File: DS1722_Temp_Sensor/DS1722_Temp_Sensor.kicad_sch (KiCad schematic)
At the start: 13 parts, among them J1 Conn_01x08, J2 Conn_01x08

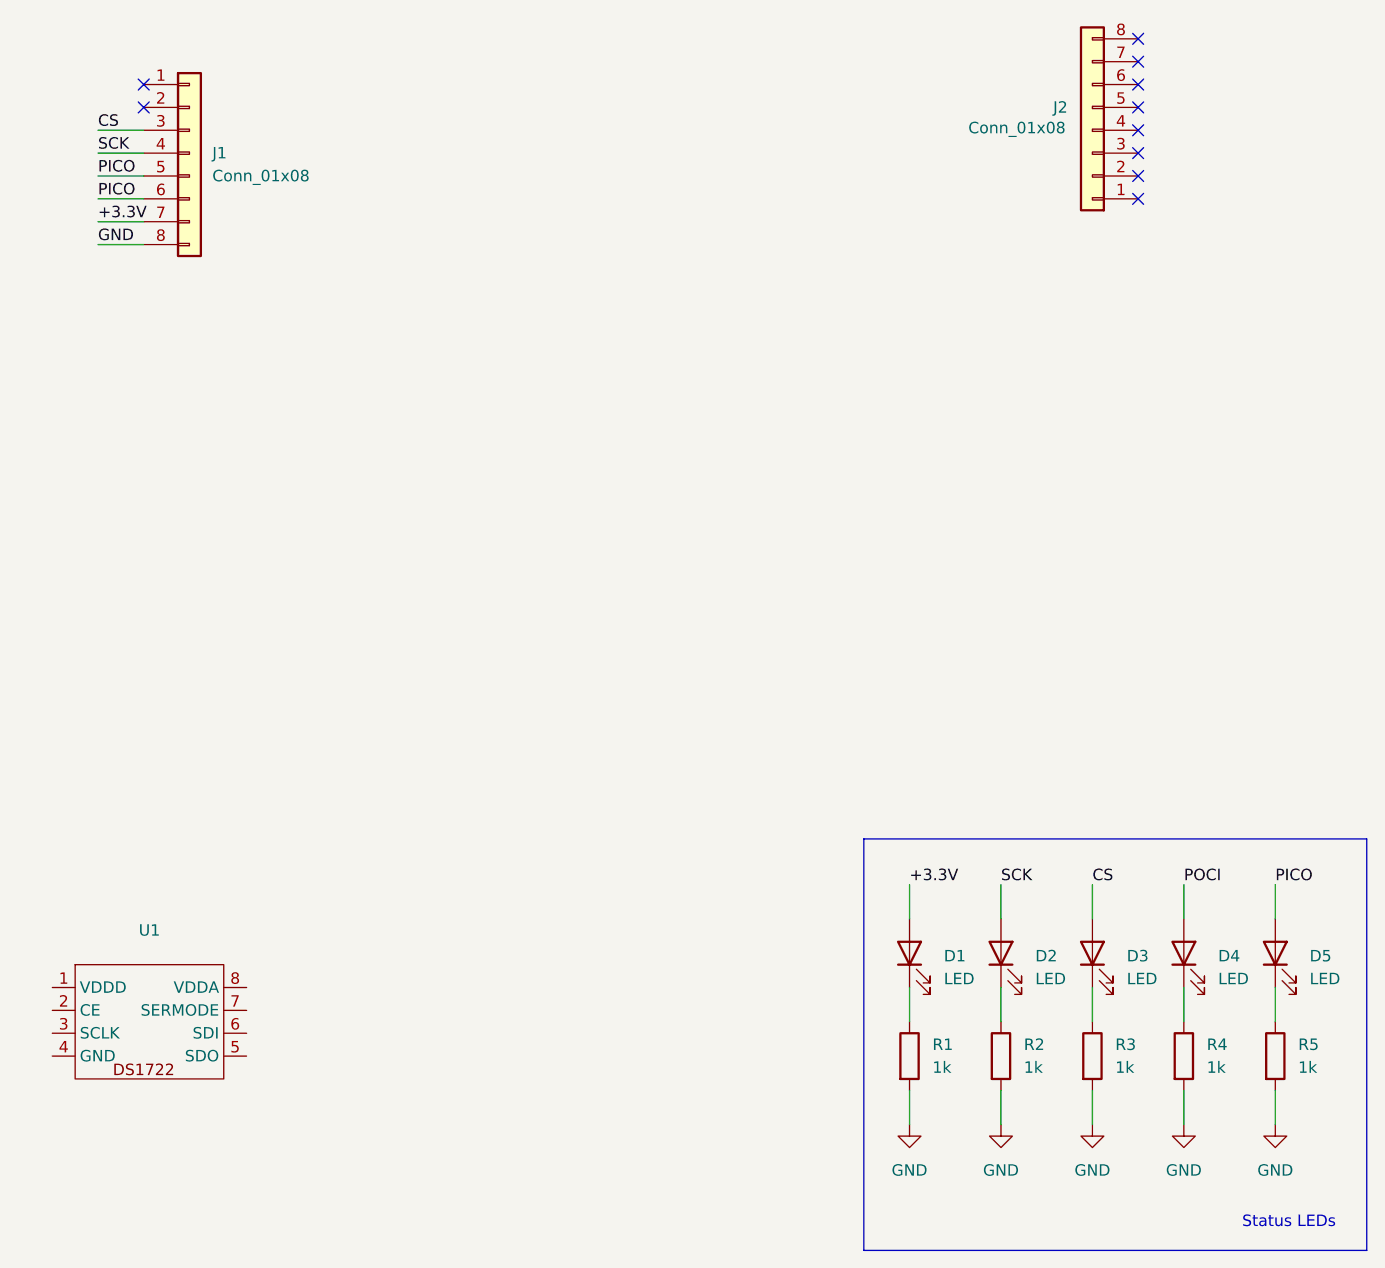
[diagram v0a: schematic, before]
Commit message: Added in labels in schematic
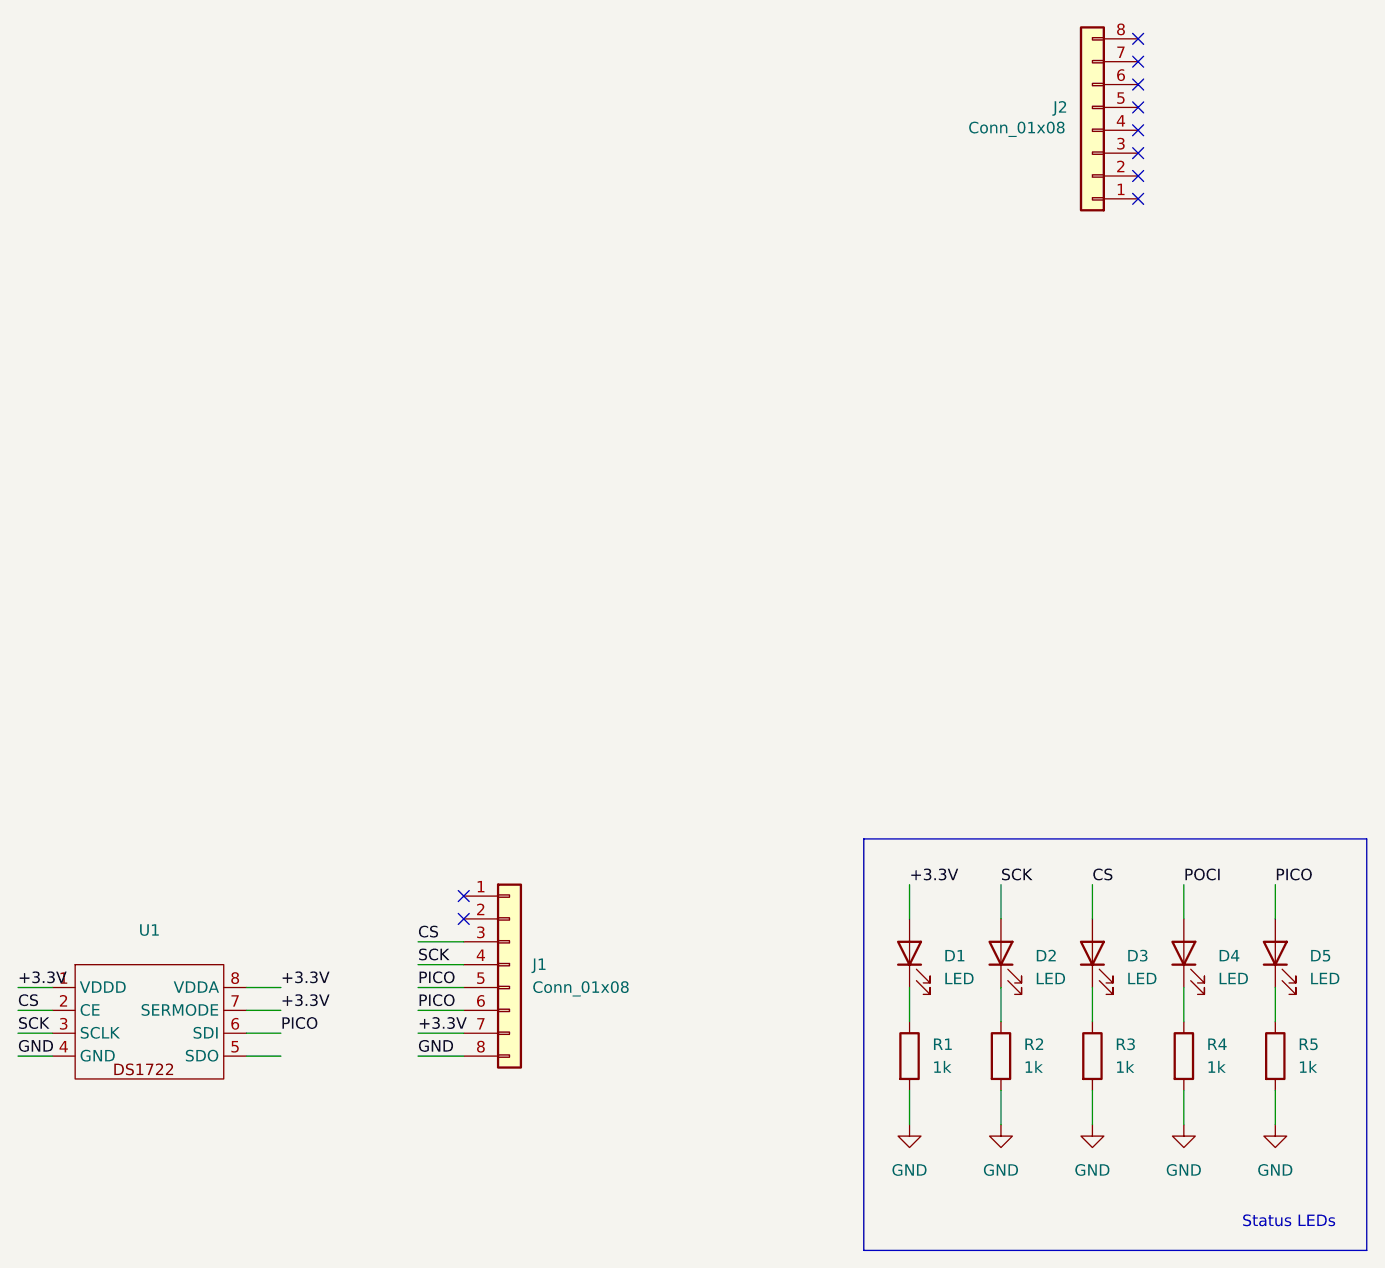
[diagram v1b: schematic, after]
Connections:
- net +3.3V: now also U1.1 (VDDD), U1.7 (SERMODE), U1.8 (VDDA)
- net CS: now also U1.2 (CE)
- net GND: now also U1.4 (GND)
- net PICO: now also U1.6 (SDI)
- net SCK: now also U1.3 (SCLK)
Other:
- moved on the sheet: J1
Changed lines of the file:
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@@
 	)
 	(no_connect
-		(at 80.01 29.21)
+		(at 115.57 119.38)
 	)
 	(no_connect
@@
 	)
 	(no_connect
-		(at 80.01 31.75)
+		(at 115.57 121.92)
 	)
 	(no_connect
@@
 	(wire
 		(pts
+			(xy 66.04 129.54) (xy 69.85 129.54)
+		)
+		(stroke
+			(width 0)
+			(type default)
+		)
+	)
+	(wire
+		(pts
 			(xy 165.1 140.97) (xy 165.1 144.78)
 		)
@@
 	(wire
 		(pts
-			(xy 74.93 34.29) (xy 80.01 34.29)
-		)
-		(stroke
-			(width 0)
-			(type default)
-		)
-	)
-	(wire
-		(pts
-			(xy 74.93 39.37) (xy 80.01 39.37)
+			(xy 110.49 124.46) (xy 115.57 124.46)
+		)
+		(stroke
+			(width 0)
+			(type default)
+		)
+	)
+	(wire
+		(pts
+			(xy 110.49 129.54) (xy 115.57 129.54)
 		)
 		(stroke
@@
 	(wire
 		(pts
-			(xy 74.93 46.99) (xy 80.01 46.99)
-		)
-		(stroke
-			(width 0)
-			(type default)
-		)
-	)
-	(wire
-		(pts
-			(xy 74.93 36.83) (xy 80.01 36.83)
+			(xy 110.49 137.16) (xy 115.57 137.16)
+		)
+		(stroke
+			(width 0)
+			(type default)
+		)
+	)
+	(wire
+		(pts
+			(xy 91.44 129.54) (xy 95.25 129.54)
+		)
+		(stroke
+			(width 0)
+			(type default)
+		)
+	)
+	(wire
+		(pts
+			(xy 110.49 127) (xy 115.57 127)
 		)
 		(stroke
@@
 	(wire
 		(pts
+			(xy 91.44 132.08) (xy 95.25 132.08)
+		)
+		(stroke
+			(width 0)
+			(type default)
+		)
+	)
+	(wire
+		(pts
 			(xy 195.58 129.54) (xy 195.58 133.35)
 		)
@@
 	(wire
 		(pts
+			(xy 66.04 132.08) (xy 69.85 132.08)
+		)
+		(stroke
+			(width 0)
+			(type default)
+		)
+	)
+	(wire
+		(pts
+			(xy 91.44 134.62) (xy 95.25 134.62)
+		)
+		(stroke
+			(width 0)
+			(type default)
+		)
+	)
+	(wire
+		(pts
 			(xy 175.26 140.97) (xy 175.26 144.78)
 		)
@@
 	(wire
 		(pts
-			(xy 74.93 41.91) (xy 80.01 41.91)
+			(xy 110.49 132.08) (xy 115.57 132.08)
 		)
 		(stroke
@@
 	(wire
 		(pts
-			(xy 74.93 44.45) (xy 80.01 44.45)
+			(xy 66.04 137.16) (xy 69.85 137.16)
+		)
+		(stroke
+			(width 0)
+			(type default)
+		)
+	)
+	(wire
+		(pts
+			(xy 110.49 134.62) (xy 115.57 134.62)
+		)
+		(stroke
+			(width 0)
+			(type default)
+		)
+	)
+	(wire
+		(pts
+			(xy 66.04 134.62) (xy 69.85 134.62)
 		)
 		(stroke
@@
 		(pts
 			(xy 195.58 140.97) (xy 195.58 144.78)
+		)
+		(stroke
+			(width 0)
+			(type default)
+		)
+	)
+	(wire
+		(pts
+			(xy 91.44 137.16) (xy 95.25 137.16)
 		)
 		(stroke
@@
 		)
 	)
+	(label "+3.3V"
+		(at 66.04 129.54 0)
+		(fields_autoplaced yes)
+		(effects
+			(font
+				(size 1.27 1.27)
+			)
+			(justify left bottom)
+		)
+	)
 	(label "PICO"
 		(at 205.74 118.11 0)
@@
 	)
 	(label "PICO"
-		(at 74.93 39.37 0)
+		(at 110.49 129.54 0)
 		(fields_autoplaced yes)
 		(effects
@@
 	)
 	(label "SCK"
-		(at 74.93 36.83 0)
+		(at 110.49 127 0)
+		(fields_autoplaced yes)
+		(effects
+			(font
+				(size 1.27 1.27)
+			)
+			(justify left bottom)
+		)
+	)
+	(label "+3.3V"
+		(at 95.25 132.08 0)
 		(fields_autoplaced yes)
 		(effects
@@
 	)
 	(label "PICO"
-		(at 74.93 41.91 0)
+		(at 110.49 132.08 0)
 		(fields_autoplaced yes)
 		(effects
@@
 	)
 	(label "+3.3V"
+		(at 95.25 129.54 0)
+		(fields_autoplaced yes)
+		(effects
+			(font
+				(size 1.27 1.27)
+			)
+			(justify left bottom)
+		)
+	)
+	(label "GND"
+		(at 66.04 137.16 0)
+		(fields_autoplaced yes)
+		(effects
+			(font
+				(size 1.27 1.27)
+			)
+			(justify left bottom)
+		)
+	)
+	(label "CS"
+		(at 66.04 132.08 0)
+		(fields_autoplaced yes)
+		(effects
+			(font
+				(size 1.27 1.27)
+			)
+			(justify left bottom)
+		)
+	)
+	(label "+3.3V"
 		(at 165.1 118.11 0)
 		(fields_autoplaced yes)
@@
 	)
 	(label "+3.3V"
-		(at 74.93 44.45 0)
+		(at 110.49 134.62 0)
 		(fields_autoplaced yes)
 		(effects
@@
 	)
 	(label "GND"
-		(at 74.93 46.99 0)
+		(at 110.49 137.16 0)
 		(fields_autoplaced yes)
 		(effects
@@
 	)
 	(label "CS"
-		(at 74.93 34.29 0)
+		(at 110.49 124.46 0)
+		(fields_autoplaced yes)
+		(effects
+			(font
+				(size 1.27 1.27)
+			)
+			(justify left bottom)
+		)
+	)
+	(label "SCK"
+		(at 66.04 134.62 0)
 		(fields_autoplaced yes)
 		(effects
@@
 	(label "CS"
 		(at 185.42 118.11 0)
+		(fields_autoplaced yes)
+		(effects
+			(font
+				(size 1.27 1.27)
+			)
+			(justify left bottom)
+		)
+	)
+	(label "PICO"
+		(at 95.25 134.62 0)
 		(fields_autoplaced yes)
 		(effects
@@
 	(symbol
 		(lib_id "Connector_Generic:Conn_01x08")
-		(at 85.09 36.83 0)
+		(at 120.65 127 0)
 		(unit 1)
 		(exclude_from_sim no)
@@
 		(fields_autoplaced yes)
 		(property "Reference" "J1"
-			(at 87.63 36.8299 0)
+			(at 123.19 126.9999 0)
 			(effects
 				(font
@@
 		)
 		(property "Value" "Conn_01x08"
-			(at 87.63 39.3699 0)
+			(at 123.19 129.5399 0)
 			(effects
 				(font
@@
 		)
 		(property "Footprint" ""
-			(at 85.09 36.83 0)
+			(at 120.65 127 0)
 			(effects
 				(font
@@
 		)
 		(property "Datasheet" "~"
-			(at 85.09 36.83 0)
+			(at 120.65 127 0)
 			(effects
 				(font
@@
 		)
 		(property "Description" "Generic connector, single row, 01x08, script generated (kicad-library-utils/schlib/autogen/connector/)"
-			(at 85.09 36.83 0)
-			(effects
-				(font
+			(at 120.65 127 0)
+			(effects
+				(font
